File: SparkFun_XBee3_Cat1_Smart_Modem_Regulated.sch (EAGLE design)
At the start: 42 parts, among them J4 QWIIC_RIGHT_ANGLE, U2 AP63203

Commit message: MOves to a smaller schematic symbol, tries to make the associate LED visible
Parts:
- removed FRAME1: FRAME-LEDGER, SparkFun-Aesthetics:FRAME-LEDGER
- added FRAME2: FRAME-LETTER, SparkFun-Aesthetics:FRAME-LETTER
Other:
- moved on the sheet: ALED, C1, C10, C2, C3, C4, C6, C7, C9, D2, D3, D4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

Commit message: MOre vias
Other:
- note added: "v01"
- note removed: "v02"
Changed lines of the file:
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@@
 <text x="195.834" y="500.126" size="2.54" layer="94" font="vector" align="center">Buck Converter - AP63203</text>
 <text x="208.28" y="426.72" size="2.54" layer="94" font="vector" align="center">Qwiic - I2C</text>
-<text x="248.92" y="327.66" size="2.54" layer="94" font="vector" align="center">v02</text>
+<text x="248.92" y="327.66" size="2.54" layer="94" font="vector" align="center">v01</text>
 <text x="187.96" y="330.2" size="2.54" layer="94" font="vector" align="center">Elias Santistevan</text>
 <text x="43.18" y="426.72" size="2.54" layer="94" font="vector" align="center">Buttons and LEDs</text>

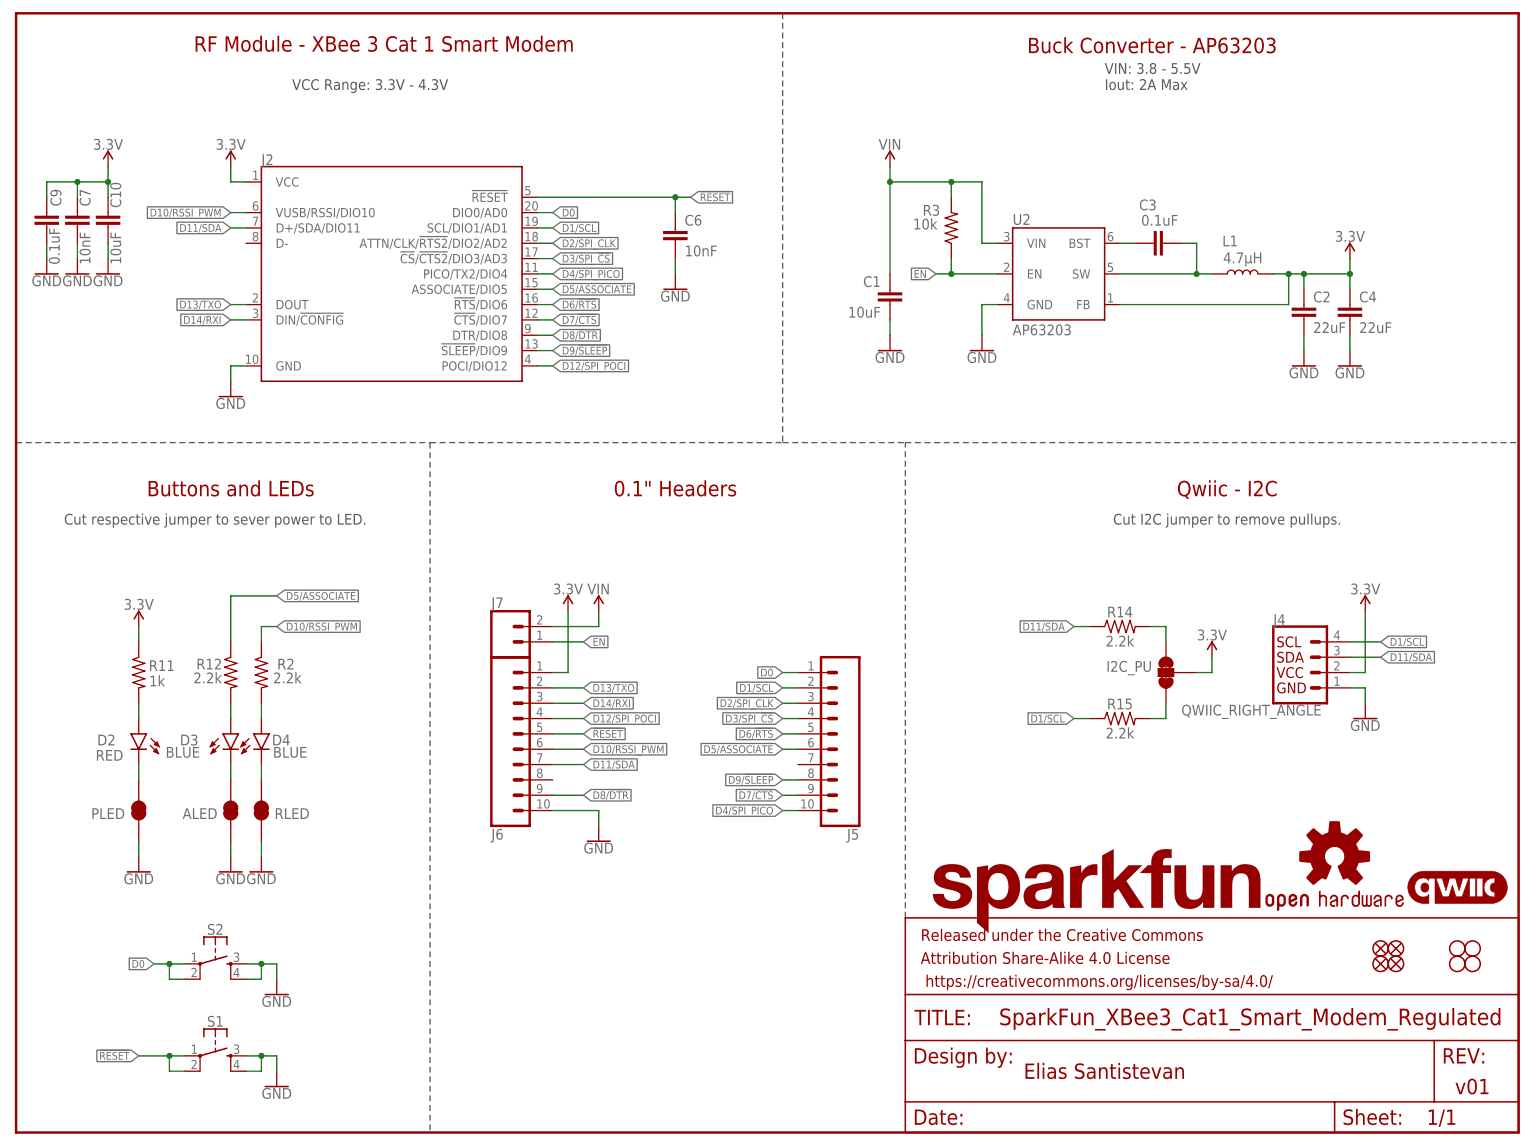
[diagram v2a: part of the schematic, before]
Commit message: Adds two additional layers, routes all nets, adds most silk
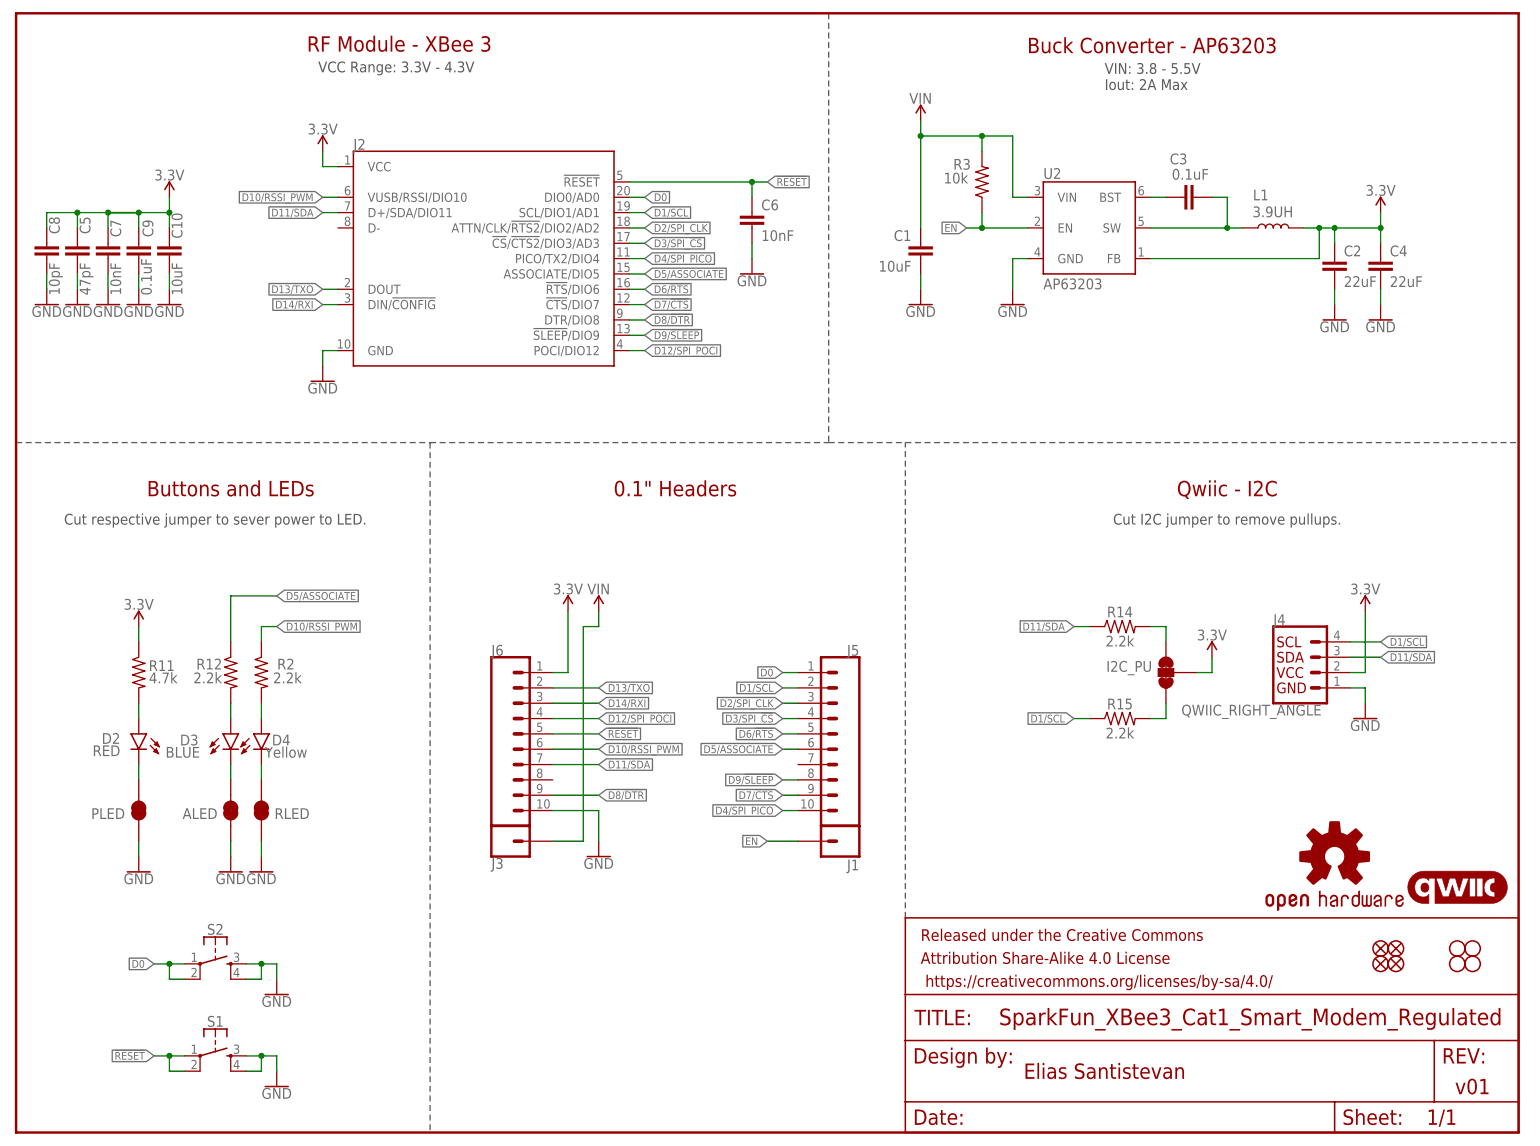
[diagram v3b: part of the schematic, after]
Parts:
- removed J7: (no value), SparkFun-Connectors:CONN_021X02_NO_SILK
- removed LOGO1: SFE_LOGO_NAME.1_INCH, SparkFun-Aesthetics:SFE_LOGO_NAME.1_INCH
- added C5: 47pF, SparkFun-Capacitors:47PF-0603-50V-5%
- added C8: 10pF, SparkFun-Capacitors:10PF-0603-50V-5%
- added J1, J3: (no value), SparkFun-Connectors:CONN_01PTH_NO_SILK_STAND
- D2: device SparkFun-LED:LED-RED0603 -> SparkFun-LED:LED-RED_0603-KB
- D4: value BLUE -> Yellow; device SparkFun-LED:LED-BLUE0603 -> SparkFun-LED:LED-YELLOW0603
- J2: device xbee_smart_modem:XBEE_UPDATEXBEE_SMD_SILK -> xbee_smart_modem:XBEE_UPDATEXBEE_SMD
- L1: value 4.7μH -> 3.9UH; device SparkFun-Coils:4.7μH_SHIELDED_INDUCTORNPIS_LS -> SparkFun-Coils:3.9UH
- LOGO3: value QWIIC_LOGO_5MM -> QWIIC_LOGO_4MM; device SparkFun-Aesthetics:QWIIC_LOGO_5MM -> SparkFun-Aesthetics:QWIIC_LOGO_4MM
- R11: value 1k -> 4.7k; device SparkFun-Resistors:1KOHM-0603-1/10W-1% -> SparkFun-Resistors:4.7KOHM-0603-1/10W-1%
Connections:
- net 3.3V: now also C5.1, C8.1
- net EN: now also J1.1; no longer J7.1
- net GND: now also C5.2, C8.2
- net VIN: now also J3.1; no longer J7.2
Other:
- note added: "RF Module - XBee 3"
- note removed: "RF Module - XBee 3 Cat 1 Smart Modem"
- moved on the sheet: C1, C10, C2, C3, C4, C6, C7, C9, J2, R3, U2

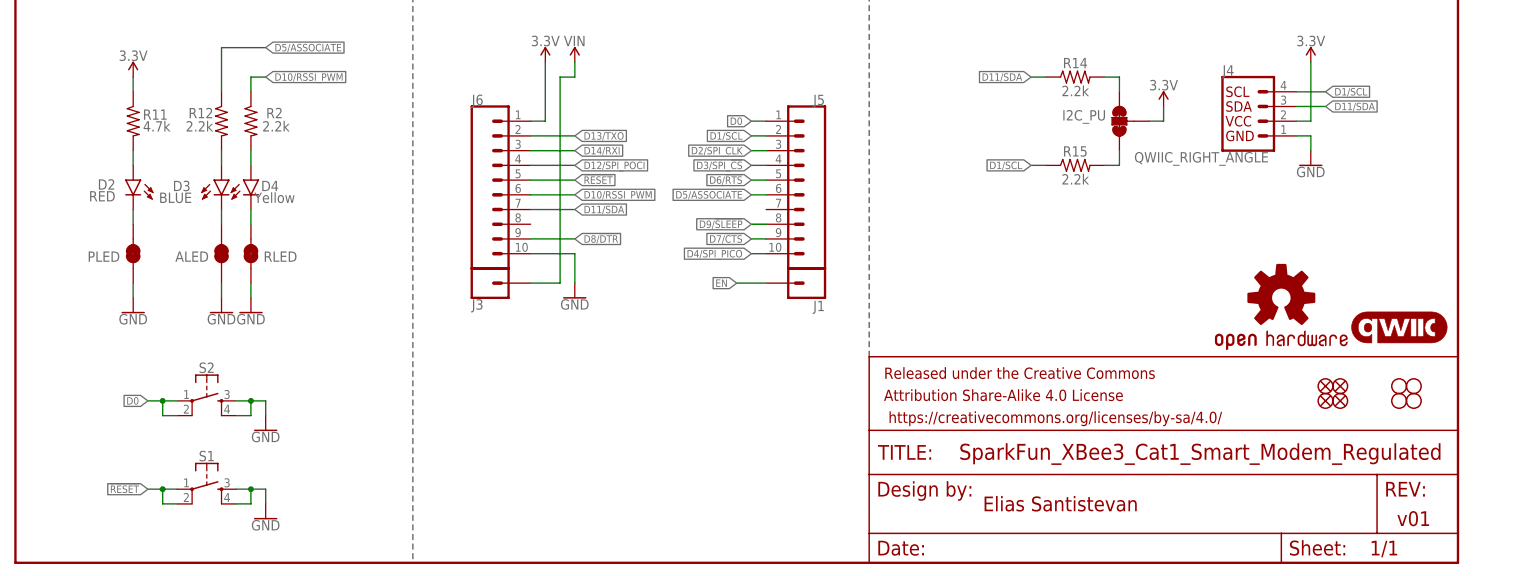
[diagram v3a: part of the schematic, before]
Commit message: Adds more silk labels,  Adds ordering instructions
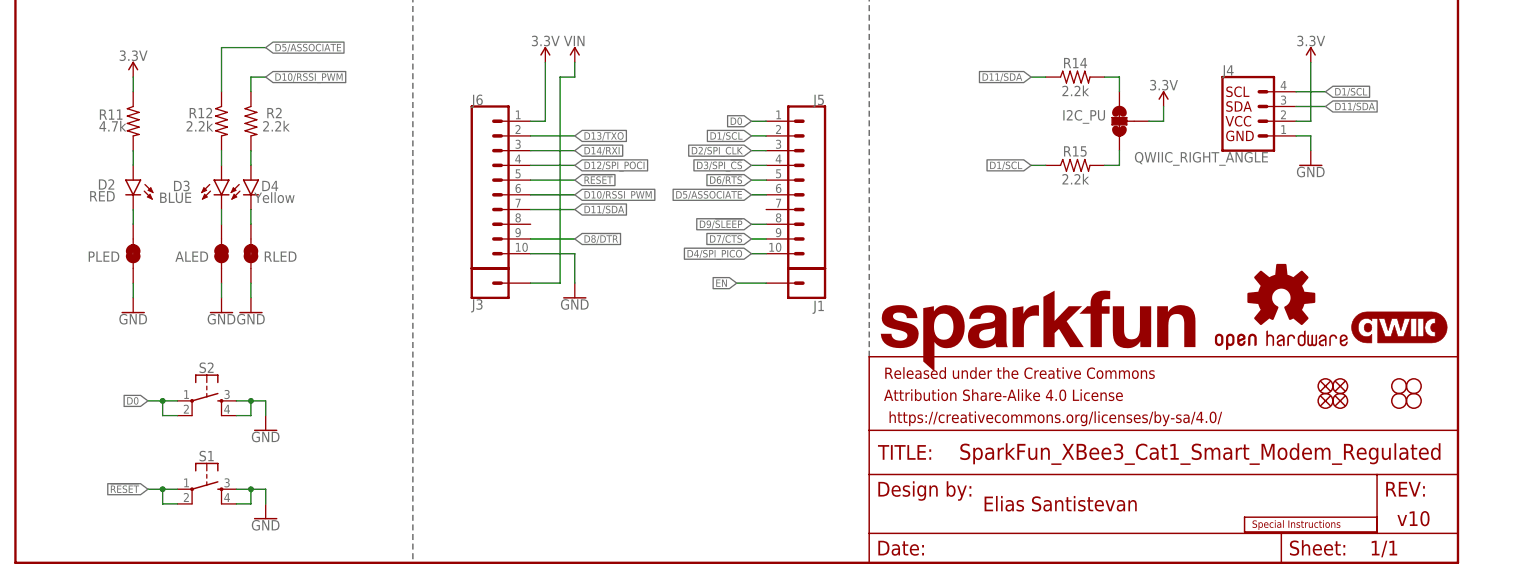
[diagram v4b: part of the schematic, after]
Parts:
- added LOGO1: SPECIAL_INSTRUCTIONS-ORDERING, SparkFun-Aesthetics:SPECIAL_INSTRUCTIONS-ORDERING
- added LOGO4: SFE_LOGO_NAMEBLANK, SparkFun-Aesthetics:SFE_LOGO_NAMEBLANK
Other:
- note added: "v10"
- note removed: "v01"
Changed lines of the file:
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@@
 <part name="GND4" library="SparkFun-PowerSymbols" deviceset="GND" device=""/>
 <part name="GND5" library="SparkFun-PowerSymbols" deviceset="GND" device=""/>
+<part name="LOGO1" library="SparkFun-Aesthetics" deviceset="SPECIAL_INSTRUCTIONS" device="-ORDERING"/>
+<part name="LOGO4" library="SparkFun-Aesthetics" deviceset="SFE_LOGO_NAME" device="BLANK"/>
 </parts>
 <sheets>
@@
 <text x="195.834" y="500.126" size="2.54" layer="94" font="vector" align="center">Buck Converter - AP63203</text>
 <text x="208.28" y="426.72" size="2.54" layer="94" font="vector" align="center">Qwiic - I2C</text>
-<text x="248.92" y="327.66" size="2.54" layer="94" font="vector" align="center">v01</text>
+<text x="248.92" y="327.66" size="2.54" layer="94" font="vector" align="center">v10</text>
 <text x="187.96" y="330.2" size="2.54" layer="94" font="vector" align="center">Elias Santistevan</text>
 <text x="43.18" y="426.72" size="2.54" layer="94" font="vector" align="center">Buttons and LEDs</text>
@@
 </instance>
 <instance part="R11" gate="G$1" x="27.94" y="396.24" smashed="yes" rot="MR270">
-<attribute name="NAME" x="31.75" y="398.272" size="1.778" layer="95" font="vector" rot="MR180" align="bottom-center"/>
-<attribute name="VALUE" x="32.004" y="394.462" size="1.778" layer="96" font="vector" rot="MR180" align="top-center"/>
+<attribute name="NAME" x="24.13" y="398.272" size="1.778" layer="95" font="vector" rot="MR180" align="bottom-center"/>
+<attribute name="VALUE" x="24.384" y="394.462" size="1.778" layer="96" font="vector" rot="MR180" align="top-center"/>
 </instance>
 <instance part="D2" gate="G$1" x="27.94" y="386.08" smashed="yes" rot="MR0">
@@
 <attribute name="VALUE" x="12.7" y="456.946" size="1.778" layer="96" font="vector" rot="MR0" align="top-center"/>
 </instance>
+<instance part="LOGO1" gate="G$1" x="219.71" y="325.374" smashed="yes"/>
+<instance part="LOGO4" gate="G$1" x="154.94" y="353.06" smashed="yes"/>
 </instances>
 <busses>
